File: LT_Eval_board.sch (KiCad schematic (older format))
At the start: 0 parts

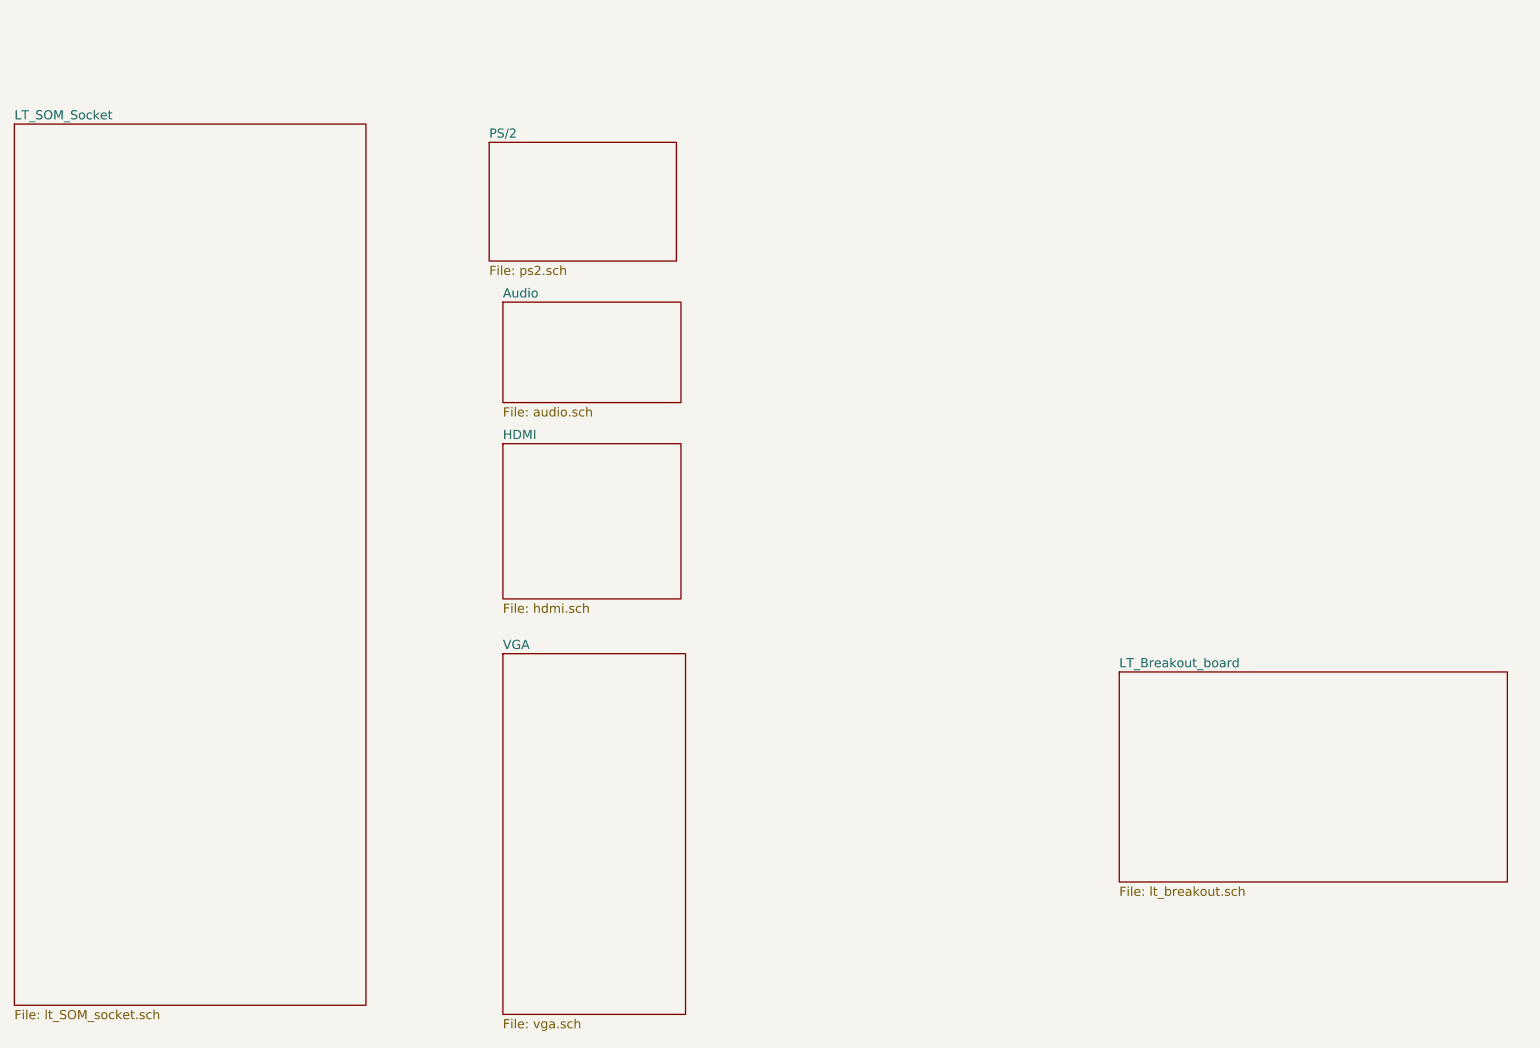
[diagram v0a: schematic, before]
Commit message: SOM added.
Signed-off-by: Kali Prasad <kprasadvnsi@protonmail.com>
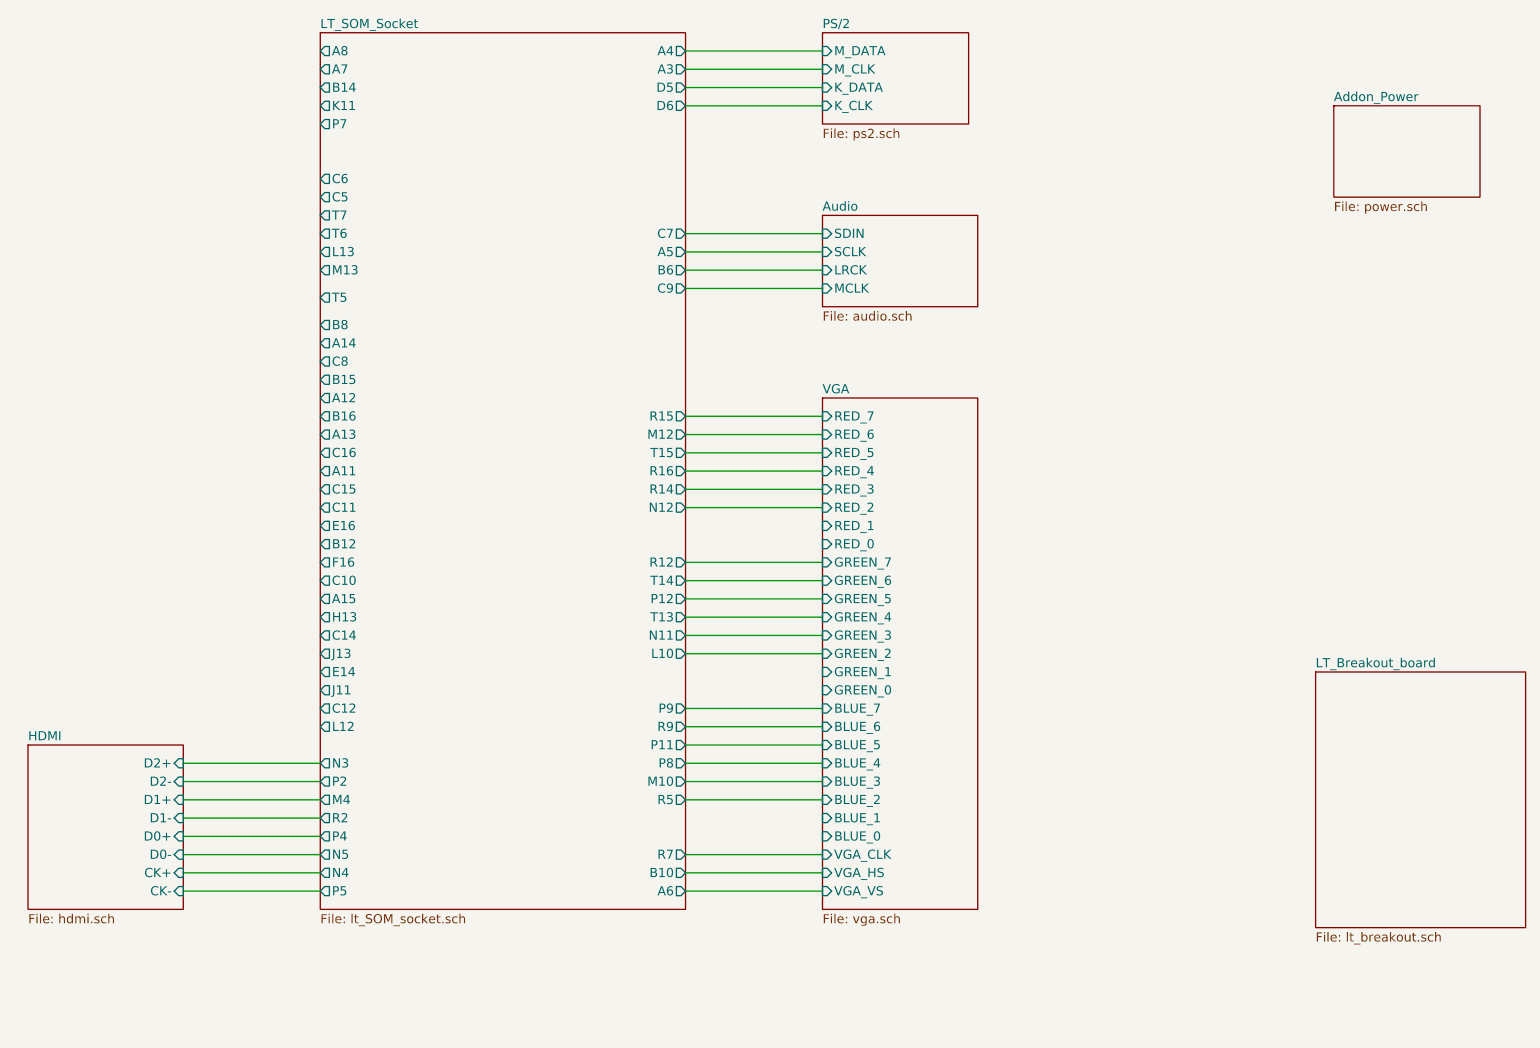
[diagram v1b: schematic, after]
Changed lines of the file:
@@
 $Descr A4 11693 8268
 encoding utf-8
-Sheet 1 7
+Sheet 1 8
 Title "LT_Eval_board"
 Date "2019-06-16"
@@
 $EndDescr
 $Sheet
-S 8075 4600 2125 1150
+S 9150 4600 1150 1400
 U 5D06776E
 F0 "LT_Breakout_board" 50
@@
 $EndSheet
 $Sheet
-S 2025 1600 1925 4825
+S 6450 2100 850  500
+U 5D067936
+F0 "Audio" 50
+F1 "audio.sch" 50
+F2 "SDIN" I L 6450 2200 50
+F3 "SCLK" I L 6450 2300 50
+F4 "LRCK" I L 6450 2400 50
+F5 "MCLK" I L 6450 2500 50
+$EndSheet
+$Sheet
+S 6450 1100 800  500
+U 5D071127
+F0 "PS/2" 50
+F1 "ps2.sch" 50
+F2 "M_DATA" I L 6450 1200 50
+F3 "M_CLK" I L 6450 1300 50
+F4 "K_DATA" I L 6450 1400 50
+F5 "K_CLK" I L 6450 1500 50
+$EndSheet
+$Sheet
+S 3700 1100 2000 4800
 U 5D0677E1
 F0 "LT_SOM_Socket" 50
 F1 "lt_SOM_socket.sch" 50
-$EndSheet
-$Sheet
-S 4700 4500 1000 1975
+F2 "A8" O L 3700 1200 50
+F3 "A7" O L 3700 1300 50
+F4 "B14" O L 3700 1400 50
+F5 "D5" O R 5700 1400 50
+F6 "A4" O R 5700 1200 50
+F7 "D6" O R 5700 1500 50
+F8 "A3" O R 5700 1300 50
+F9 "C6" O L 3700 1900 50
+F10 "C5" O L 3700 2000 50
+F11 "C7" O R 5700 2200 50
+F12 "B6" O R 5700 2400 50
+F13 "A5" O R 5700 2300 50
+F14 "C9" O R 5700 2500 50
+F15 "A6" O R 5700 5800 50
+F16 "B10" O R 5700 5700 50
+F17 "B8" O L 3700 2700 50
+F18 "A14" O L 3700 2800 50
+F19 "C8" O L 3700 2900 50
+F20 "B15" O L 3700 3000 50
+F21 "A12" O L 3700 3100 50
+F22 "B16" O L 3700 3200 50
+F23 "A13" O L 3700 3300 50
+F24 "C16" O L 3700 3400 50
+F25 "A11" O L 3700 3500 50
+F26 "C15" O L 3700 3600 50
+F27 "C11" O L 3700 3700 50
+F28 "E16" O L 3700 3800 50
+F29 "B12" O L 3700 3900 50
+F30 "F16" O L 3700 4000 50
+F31 "C10" O L 3700 4100 50
+F32 "A15" O L 3700 4200 50
+F33 "H13" O L 3700 4300 50
+F34 "C14" O L 3700 4400 50
+F35 "J13" O L 3700 4500 50
+F36 "E14" O L 3700 4600 50
+F37 "J11" O L 3700 4700 50
+F38 "C12" O L 3700 4800 50
+F39 "L12" O L 3700 4900 50
+F40 "N3" O L 3700 5100 50
+F41 "P2" O L 3700 5200 50
+F42 "M4" O L 3700 5300 50
+F43 "R2" O L 3700 5400 50
+F44 "P4" O L 3700 5500 50
+F45 "N5" O L 3700 5600 50
+F46 "N4" O L 3700 5700 50
+F47 "P5" O L 3700 5800 50
+F48 "T5" O L 3700 2550 50
+F49 "T7" O L 3700 2100 50
+F50 "T6" O L 3700 2200 50
+F51 "R7" O R 5700 5600 50
+F52 "R5" O R 5700 5300 50
+F53 "P8" O R 5700 5100 50
+F54 "M10" O R 5700 5200 50
+F55 "R9" O R 5700 4900 50
+F56 "P11" O R 5700 5000 50
+F57 "P9" O R 5700 4800 50
+F58 "L10" O R 5700 4500 50
+F59 "T13" O R 5700 4300 50
+F60 "N11" O R 5700 4400 50
+F61 "T14" O R 5700 4100 50
+F62 "P12" O R 5700 4200 50
+F63 "R12" O R 5700 4000 50
+F64 "N12" O R 5700 3700 50
+F65 "R14" O R 5700 3600 50
+F66 "R16" O R 5700 3500 50
+F67 "T15" O R 5700 3400 50
+F68 "M12" O R 5700 3300 50
+F69 "R15" O R 5700 3200 50
+F70 "L13" O L 3700 2300 50
+F71 "M13" O L 3700 2400 50
+F72 "P7" O L 3700 1600 50
+F73 "K11" O L 3700 1500 50
+$EndSheet
+Wire Wire Line
+	5700 5800 6450 5800
+Wire Wire Line
+	5700 5700 6450 5700
+Wire Wire Line
+	5700 5600 6450 5600
+Wire Wire Line
+	5700 4800 6450 4800
+Wire Wire Line
+	5700 4900 6450 4900
+Wire Wire Line
+	5700 5000 6450 5000
+Wire Wire Line
+	5700 5100 6450 5100
+Wire Wire Line
+	5700 5200 6450 5200
+Wire Wire Line
+	5700 5300 6450 5300
+Wire Wire Line
+	5700 4000 6450 4000
+Wire Wire Line
+	5700 4100 6450 4100
+Wire Wire Line
+	5700 4200 6450 4200
+Wire Wire Line
+	5700 4300 6450 4300
+Wire Wire Line
+	5700 4400 6450 4400
+Wire Wire Line
+	5700 4500 6450 4500
+Wire Wire Line
+	5700 3200 6450 3200
+Wire Wire Line
+	5700 3300 6450 3300
+Wire Wire Line
+	5700 3400 6450 3400
+Wire Wire Line
+	5700 3500 6450 3500
+Wire Wire Line
+	5700 3600 6450 3600
+Wire Wire Line
+	5700 3700 6450 3700
+Wire Wire Line
+	5700 2200 6450 2200
+Wire Wire Line
+	5700 2300 6450 2300
+Wire Wire Line
+	5700 2400 6450 2400
+Wire Wire Line
+	5700 2500 6450 2500
+$Sheet
+S 2100 5000 850  900
+U 5D0678E5
+F0 "HDMI" 50
+F1 "hdmi.sch" 50
+F2 "D2+" I R 2950 5100 50
+F3 "D2-" I R 2950 5200 50
+F4 "D1+" I R 2950 5300 50
+F5 "D1-" I R 2950 5400 50
+F6 "D0+" I R 2950 5500 50
+F7 "D0-" I R 2950 5600 50
+F8 "CK+" I R 2950 5700 50
+F9 "CK-" I R 2950 5800 50
+$EndSheet
+Wire Wire Line
+	2950 5100 3700 5100
+Wire Wire Line
+	2950 5200 3700 5200
+Wire Wire Line
+	2950 5300 3700 5300
+Wire Wire Line
+	2950 5400 3700 5400
+Wire Wire Line
+	2950 5500 3700 5500
+Wire Wire Line
+	2950 5600 3700 5600
+Wire Wire Line
+	2950 5700 3700 5700
+Wire Wire Line
+	2950 5800 3700 5800
+Wire Wire Line
+	5700 1200 6450 1200
+Wire Wire Line
+	5700 1300 6450 1300
+Wire Wire Line
+	5700 1400 6450 1400
+Wire Wire Line
+	5700 1500 6450 1500
+$Sheet
+S 6450 3100 850  2800
 U 5D06789A
 F0 "VGA" 50
 F1 "vga.sch" 50
-$EndSheet
-$Sheet
-S 4700 3350 975  850
-U 5D0678E5
-F0 "HDMI" 50
-F1 "hdmi.sch" 50
-$EndSheet
-$Sheet
-S 4700 2575 975  550
-U 5D067936
-F0 "Audio" 50
-F1 "audio.sch" 50
-$EndSheet
-$Sheet
-S 4625 1700 1025 650
-U 5D071127
-F0 "PS/2" 50
-F1 "ps2.sch" 50
+F2 "RED_6" I L 6450 3300 50
+F3 "RED_5" I L 6450 3400 50
+F4 "RED_4" I L 6450 3500 50
+F5 "RED_3" I L 6450 3600 50
+F6 "RED_2" I L 6450 3700 50
+F7 "RED_7" I L 6450 3200 50
+F8 "RED_1" I L 6450 3800 50
+F9 "RED_0" I L 6450 3900 50
+F10 "GREEN_7" I L 6450 4000 50
+F11 "GREEN_6" I L 6450 4100 50
+F12 "GREEN_5" I L 6450 4200 50
+F13 "GREEN_4" I L 6450 4300 50
+F14 "GREEN_3" I L 6450 4400 50
+F15 "GREEN_2" I L 6450 4500 50
+F16 "GREEN_0" I L 6450 4700 50
+F17 "GREEN_1" I L 6450 4600 50
+F18 "BLUE_7" I L 6450 4800 50
+F19 "BLUE_6" I L 6450 4900 50
+F20 "BLUE_5" I L 6450 5000 50
+F21 "BLUE_4" I L 6450 5100 50
+F22 "BLUE_3" I L 6450 5200 50
+F23 "BLUE_2" I L 6450 5300 50
+F24 "VGA_CLK" I L 6450 5600 50
+F25 "BLUE_0" I L 6450 5500 50
+F26 "BLUE_1" I L 6450 5400 50
+F27 "VGA_HS" I L 6450 5700 50
+F28 "VGA_VS" I L 6450 5800 50
+$EndSheet
+$Sheet
+S 9250 1500 800  500
+U 5D1775F8
+F0 "Addon_Power" 50
+F1 "power.sch" 50
 $EndSheet
 $EndSCHEMATC
